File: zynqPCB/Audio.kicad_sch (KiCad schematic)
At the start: 38 parts, among them Q10 IRLML2502, Q5 IRLML2502, Q6 IRLML2502, Q7 IRLML2502, Q8 IRLML2502, Q9 IRLML2502, U20 xc7z020clg484

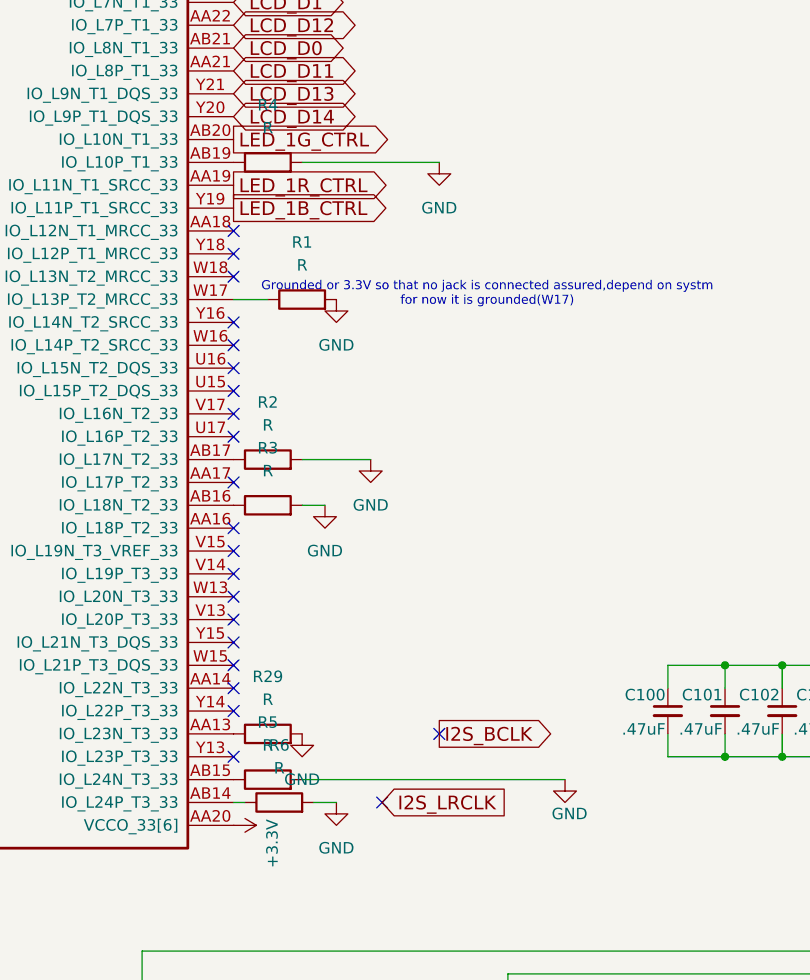
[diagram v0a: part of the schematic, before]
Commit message: sensor changed
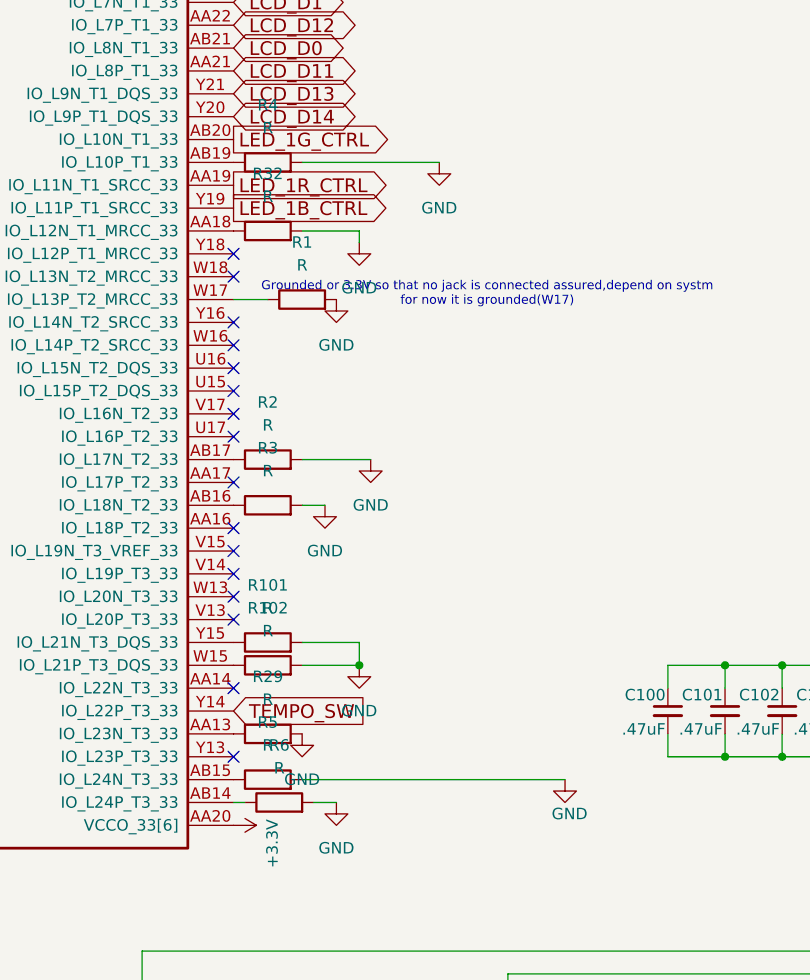
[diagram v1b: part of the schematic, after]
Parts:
- added R101, R102, R32: R, symbol DFTCustom:R
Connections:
- net GND: now also R101.2, R102.2, R32.2
- net at U20.AA18 (IO_L12N_T1_MRCC_33): now also R32.1
- net at U20.W15 (IO_L21P_T3_DQS_33): now also R102.1
- net TEMPO_SW: now reaches U20.Y14 (IO_L22P_T3_33)
- net at U20.Y15 (IO_L21N_T3_DQS_33): now also R101.1
- no-connect marks 27 -> 21
